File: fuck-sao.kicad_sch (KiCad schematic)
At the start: 31 parts, among them J1 Conn_01x03_Pin, J2 Conn_02x03_Odd_Even, SW1 SW_Push, U1 ATtiny416-M

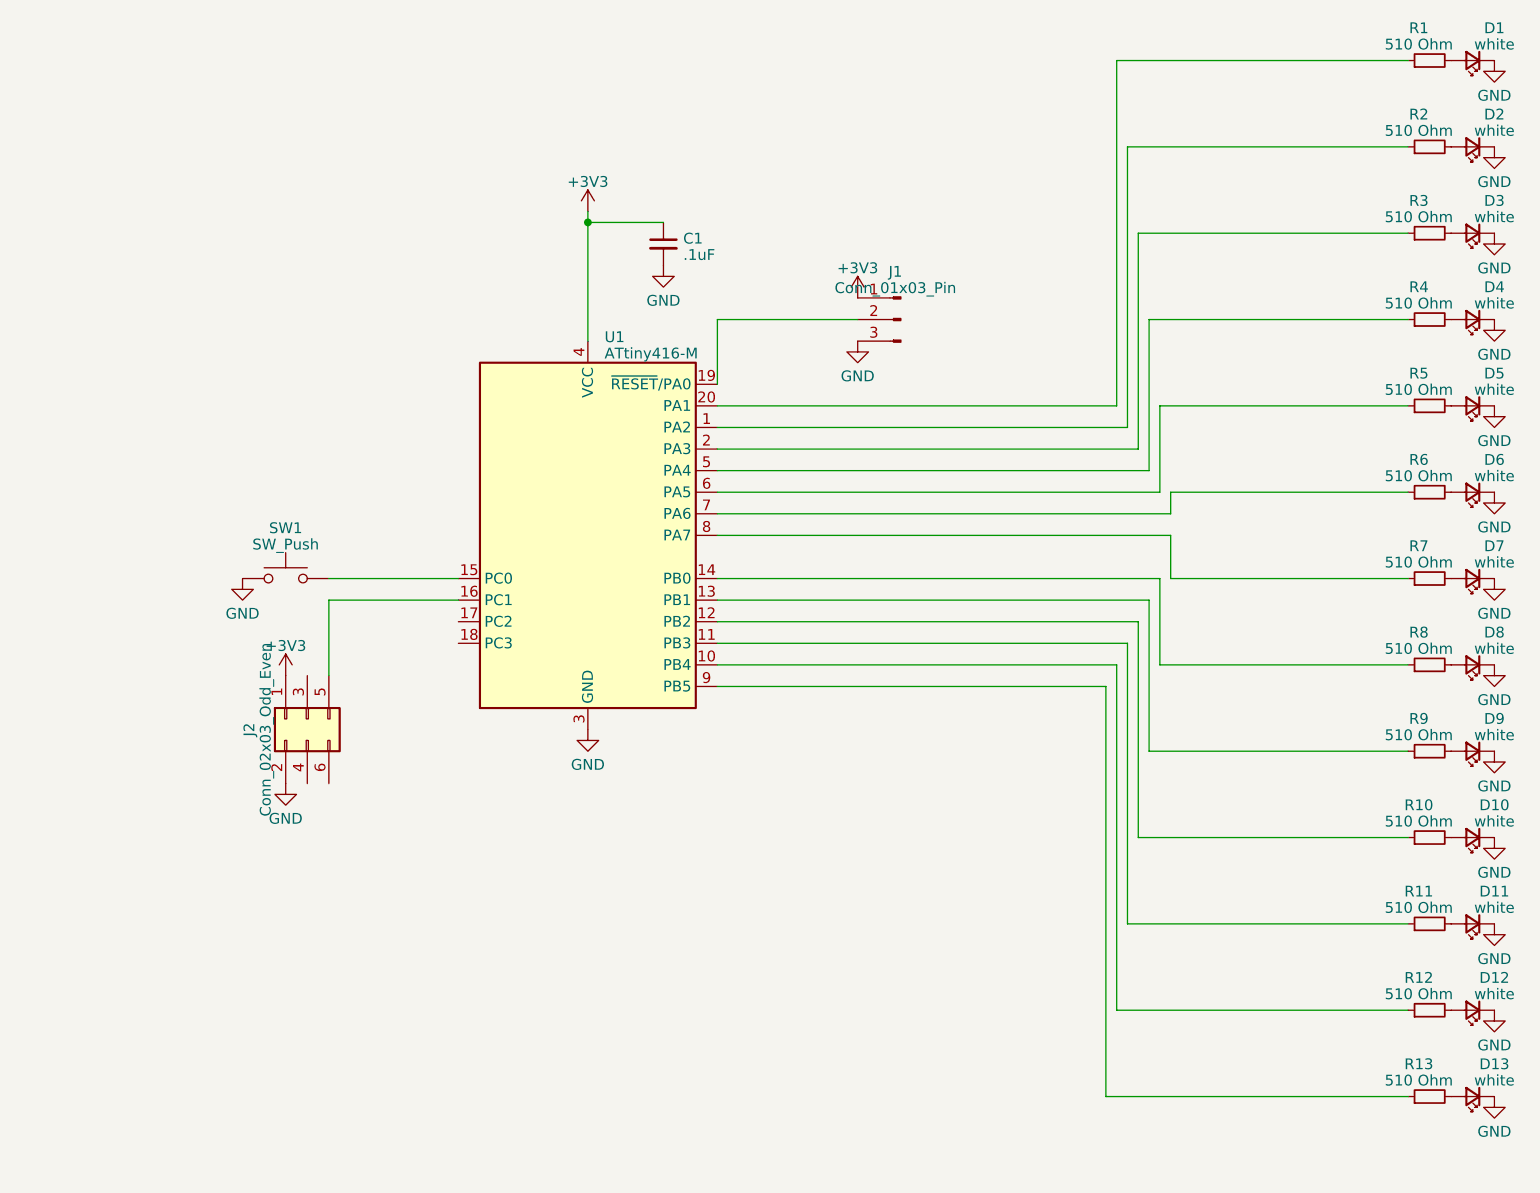
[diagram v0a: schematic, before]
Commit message: new touch program and new board desigh
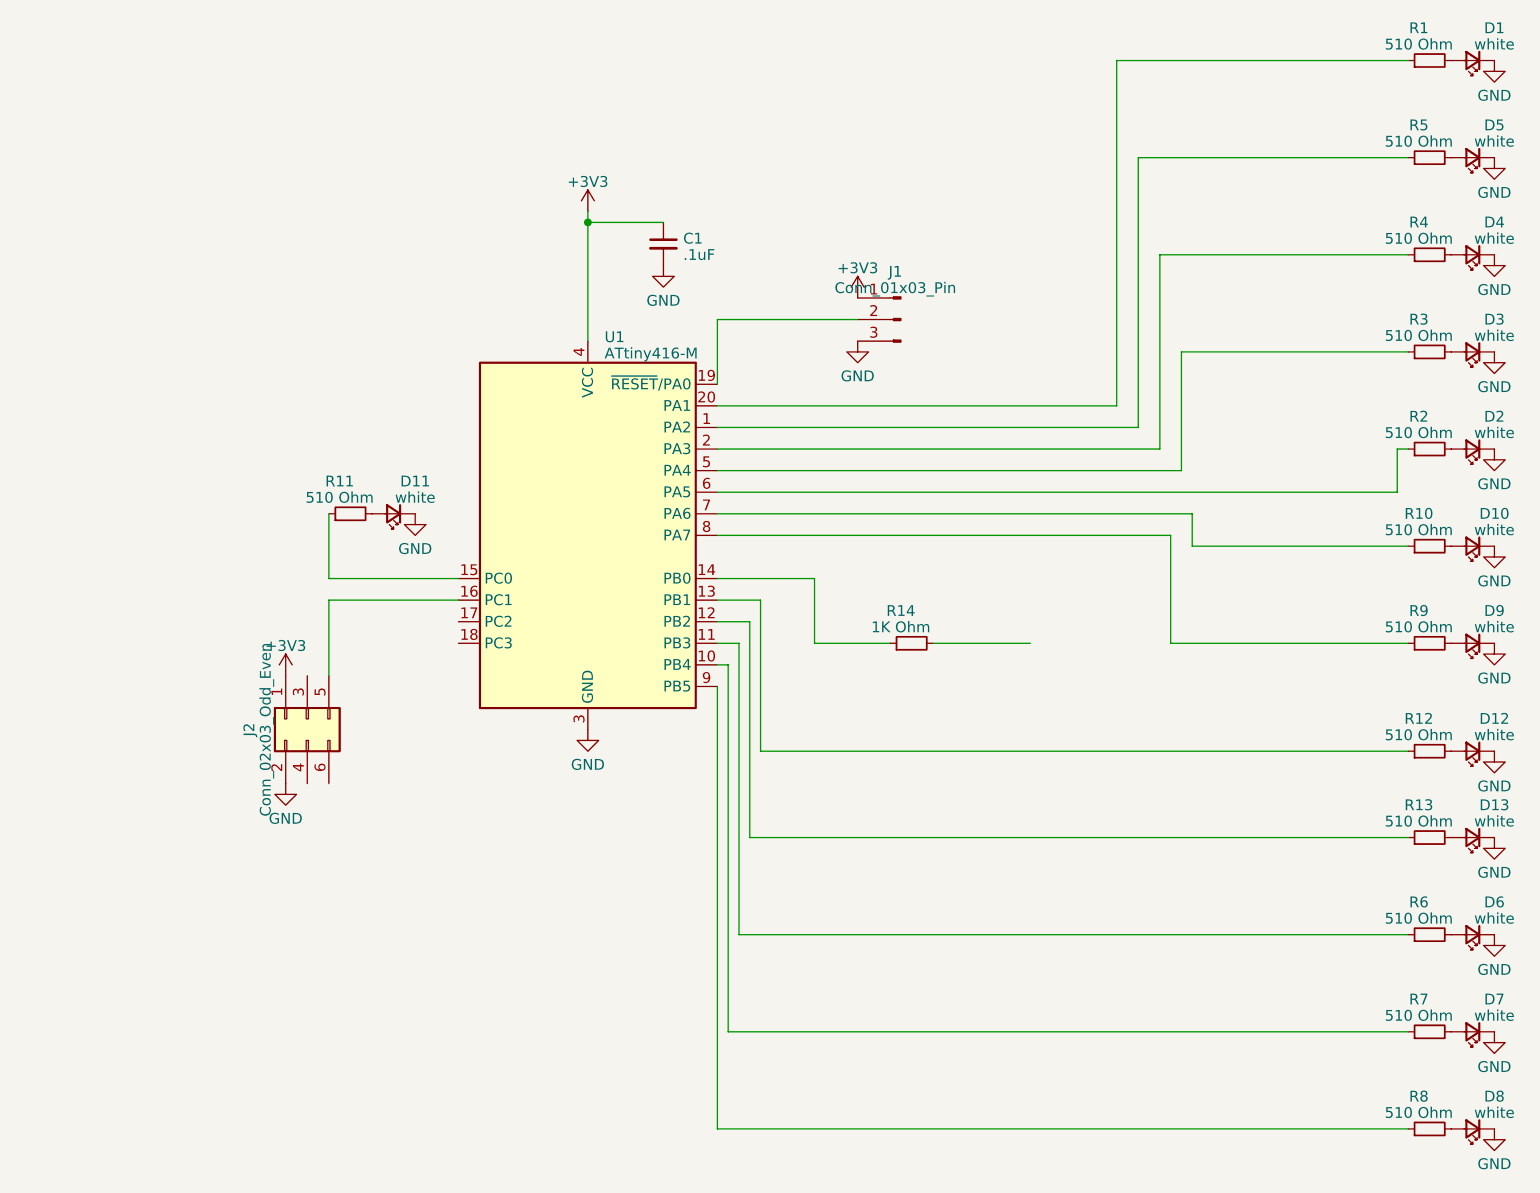
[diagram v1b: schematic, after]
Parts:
- removed SW1: SW_Push, Button_Switch_SMD:SW_Tactile_SPST_NO_Straight_CK_PTS636Sx25SMTRLFS, symbol Switch:SW_Push
- added R14: 1K Ohm, Resistor_SMD:R_0603_1608Metric, symbol Device:R_Small
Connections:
- net at U1.15 (PC0): now also R11.1
- net at R6.1: now also U1.11 (PB3); no longer U1.7 (PA6)
- net at R8.1: now also U1.9 (PB5); no longer U1.14 (PB0)
- net at R4.1: now also U1.2 (PA3); no longer U1.5 (PA4)
- net at R12.1: now also U1.13 (PB1); no longer U1.10 (PB4)
- net at R5.1: now also U1.1 (PA2); no longer U1.6 (PA5)
- net at R9.1: now also U1.8 (PA7); no longer U1.13 (PB1)
- net at R7.1: now also U1.10 (PB4); no longer U1.8 (PA7)
- net at R3.1: now also U1.5 (PA4); no longer U1.2 (PA3)
- net at R2.1: now also U1.6 (PA5); no longer U1.1 (PA2)
- net at R10.1: now also U1.7 (PA6); no longer U1.12 (PB2)
- net at R13.1: now also U1.12 (PB2); no longer U1.9 (PB5)
- new net: R14.1, U1.14 (PB0)
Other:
- moved on the sheet: D10, D11, D12, D13, D2, D3, D4, D5, D6, D7, D8, D9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

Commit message: media and more
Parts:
- added BT1: Battery_Cell, symbol Device:Battery_Cell
- added SW1: SW_Nidec_CAS-120A1, Button_Switch_SMD:Nidec_Copal_CAS-120A, symbol Switch:SW_Nidec_CAS-120A1
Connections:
- net +3V3: now also SW1.3 (A)
- net GND: now also BT1.2 (-)
- new net: BT1.1 (+), SW1.2 (B)
